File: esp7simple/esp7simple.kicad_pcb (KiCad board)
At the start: 2 copper layers, 13 parts, among them J1 Conn_01x02_Female, J2 , J3 , U1 ESP-07v2, U2 AMS1117-3.3

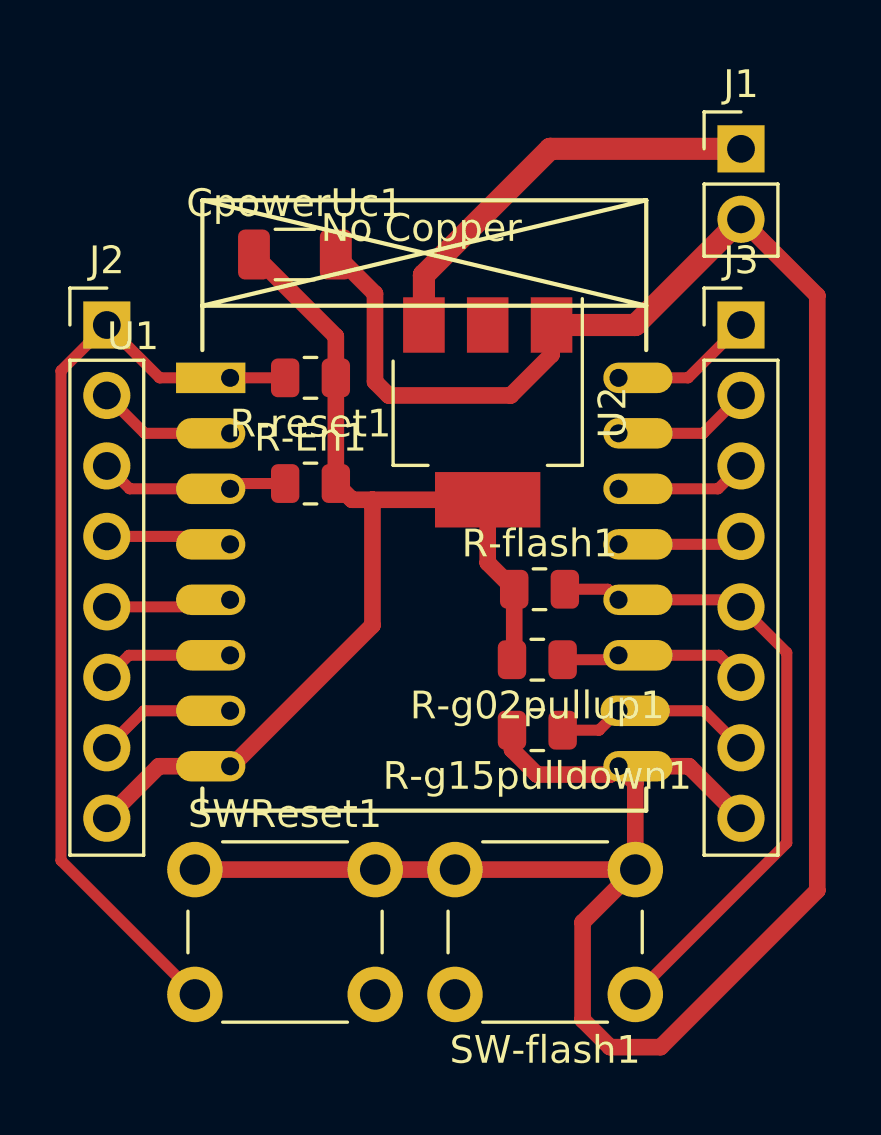
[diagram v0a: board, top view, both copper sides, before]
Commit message: add esp7 simple variant
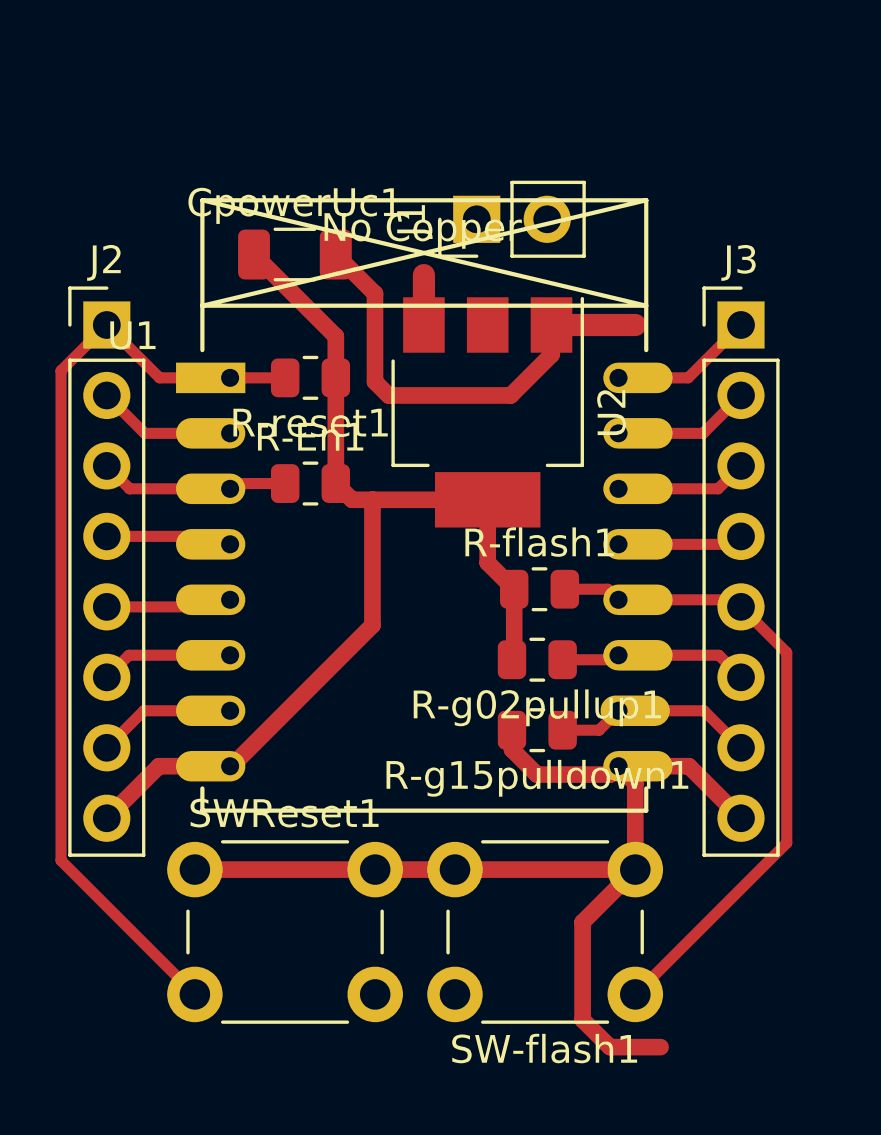
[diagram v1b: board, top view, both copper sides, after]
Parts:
- moved J1 9.86 mm to (154.9, 130.2), turned to 90 degrees
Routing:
- net GND: track 94.6 -> 55.9 mm
- net Net-(J1-Pad1): track 15.1 -> 1.80 mm
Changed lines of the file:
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@@
     (thickness 1.6)
     (drawings 0)
-    (tracks 86)
+    (tracks 80)
     (zones 0)
     (modules 13)
@@
   )
   (module Connector_PinHeader_2.54mm:PinHeader_1x02_P2.54mm_Vertical (layer F.Cu)
-    (at 164.465 127.635)
+    (at 154.94 130.175 90)
     (descr "Through hole straight pin header, 1x02, 2.54mm pitch, single row")
     (tags "Through hole pin header THT 1x02 2.54mm single row")
-    (fp_text reference J1 (at 0 -2.33) (layer F.SilkS)
-      (effects (font (size 1 1) (thickness 0.15)))
-    )
-    (fp_text value Conn_01x02_Female (at 2.54 6.35) (layer F.Fab) hide
+    (fp_text reference J1 (at 0 -2.33 90) (layer F.SilkS)
+      (effects (font (size 1 1) (thickness 0.15)))
+    )
+    (fp_text value Conn_01x02_Female (at 2.54 6.35 90) (layer F.Fab) hide
       (effects (font (size 1 1) (thickness 0.15)))
     )
@@
     (fp_line (start 1.27 -1.27) (end 1.27 3.81) (layer F.Fab) (width 0.1))
     (fp_line (start -0.635 -1.27) (end 1.27 -1.27) (layer F.Fab) (width 0.1))
-    (fp_text user %R (at 0 1.27 -270) (layer F.Fab)
-      (effects (font (size 1 1) (thickness 0.15)))
-    )
-    (pad 2 thru_hole oval (at 0 2.54) (size 1.7 1.7) (drill 1) (layers *.Cu *.Mask)
-      (net 1 GND))
-    (pad 1 thru_hole rect (at 0 0) (size 1.7 1.7) (drill 1) (layers *.Cu *.Mask)
+    (fp_text user %R (at 0 1.27) (layer F.Fab)
+      (effects (font (size 1 1) (thickness 0.15)))
+    )
+    (pad 2 thru_hole oval (at 0 2.54 90) (size 1.7 1.7) (drill 1) (layers *.Cu *.Mask)
+      (net 1 GND))
+    (pad 1 thru_hole rect (at 0 0 90) (size 1.7 1.7) (drill 1) (layers *.Cu *.Mask)
       (net 3 "Net-(J1-Pad1)"))
     (model ${KISYS3DMOD}/Connector_PinHeader_2.54mm.3dshapes/PinHeader_1x02_P2.54mm_Vertical.wrl
@@
       (effects (font (size 0.5 0.5) (thickness 0.08)))
     )
-    (pad 2 smd roundrect (at 0.9125 0 180) (size 1.025 1.4) (layers F.Cu F.Paste F.Mask) (roundrect_rratio 0.243902)
+    (pad 2 smd roundrect (at 0.9125 0 180) (size 1.025 1.4) (layers F.Cu F.Paste F.Mask) (roundrect_rratio 0.2439014634146341)
       (net 10 "Net-(J2-Pad1)"))
-    (pad 1 smd roundrect (at -0.9125 0 180) (size 1.025 1.4) (layers F.Cu F.Paste F.Mask) (roundrect_rratio 0.243902)
+    (pad 1 smd roundrect (at -0.9125 0 180) (size 1.025 1.4) (layers F.Cu F.Paste F.Mask) (roundrect_rratio 0.2439014634146341)
       (net 2 v3.3))
     (model ${KISYS3DMOD}/Resistor_SMD.3dshapes/R_0805_2012Metric.wrl
@@
       (effects (font (size 0.5 0.5) (thickness 0.08)))
     )
-    (pad 2 smd roundrect (at 0.9125 0 180) (size 1.025 1.4) (layers F.Cu F.Paste F.Mask) (roundrect_rratio 0.243902)
-      (net 1 GND))
-    (pad 1 smd roundrect (at -0.9125 0 180) (size 1.025 1.4) (layers F.Cu F.Paste F.Mask) (roundrect_rratio 0.243902)
+    (pad 2 smd roundrect (at 0.9125 0 180) (size 1.025 1.4) (layers F.Cu F.Paste F.Mask) (roundrect_rratio 0.2439014634146341)
+      (net 1 GND))
+    (pad 1 smd roundrect (at -0.9125 0 180) (size 1.025 1.4) (layers F.Cu F.Paste F.Mask) (roundrect_rratio 0.2439014634146341)
       (net 11 "Net-(J3-Pad7)"))
     (model ${KISYS3DMOD}/Resistor_SMD.3dshapes/R_0805_2012Metric.wrl
@@
       (effects (font (size 0.5 0.5) (thickness 0.08)))
     )
-    (pad 2 smd roundrect (at 0.9125 0 180) (size 1.025 1.4) (layers F.Cu F.Paste F.Mask) (roundrect_rratio 0.243902)
-      (net 2 v3.3))
-    (pad 1 smd roundrect (at -0.9125 0 180) (size 1.025 1.4) (layers F.Cu F.Paste F.Mask) (roundrect_rratio 0.243902)
+    (pad 2 smd roundrect (at 0.9125 0 180) (size 1.025 1.4) (layers F.Cu F.Paste F.Mask) (roundrect_rratio 0.2439014634146341)
+      (net 2 v3.3))
+    (pad 1 smd roundrect (at -0.9125 0 180) (size 1.025 1.4) (layers F.Cu F.Paste F.Mask) (roundrect_rratio 0.2439014634146341)
       (net 12 "Net-(J3-Pad6)"))
     (model ${KISYS3DMOD}/Resistor_SMD.3dshapes/R_0805_2012Metric.wrl
@@
       (effects (font (size 0.5 0.5) (thickness 0.08)))
     )
-    (pad 2 smd roundrect (at 0.9125 0) (size 1.025 1.4) (layers F.Cu F.Paste F.Mask) (roundrect_rratio 0.243902)
+    (pad 2 smd roundrect (at 0.9125 0) (size 1.025 1.4) (layers F.Cu F.Paste F.Mask) (roundrect_rratio 0.2439014634146341)
       (net 13 "Net-(J3-Pad5)"))
-    (pad 1 smd roundrect (at -0.9125 0) (size 1.025 1.4) (layers F.Cu F.Paste F.Mask) (roundrect_rratio 0.243902)
+    (pad 1 smd roundrect (at -0.9125 0) (size 1.025 1.4) (layers F.Cu F.Paste F.Mask) (roundrect_rratio 0.2439014634146341)
       (net 2 v3.3))
     (model ${KISYS3DMOD}/Resistor_SMD.3dshapes/R_0805_2012Metric.wrl
@@
       (effects (font (size 0.5 0.5) (thickness 0.08)))
     )
-    (pad 2 smd roundrect (at 0.9125 0) (size 1.025 1.4) (layers F.Cu F.Paste F.Mask) (roundrect_rratio 0.243902)
-      (net 2 v3.3))
-    (pad 1 smd roundrect (at -0.9125 0) (size 1.025 1.4) (layers F.Cu F.Paste F.Mask) (roundrect_rratio 0.243902)
+    (pad 2 smd roundrect (at 0.9125 0) (size 1.025 1.4) (layers F.Cu F.Paste F.Mask) (roundrect_rratio 0.2439014634146341)
+      (net 2 v3.3))
+    (pad 1 smd roundrect (at -0.9125 0) (size 1.025 1.4) (layers F.Cu F.Paste F.Mask) (roundrect_rratio 0.2439014634146341)
       (net 8 "Net-(J2-Pad3)"))
     (model ${KISYS3DMOD}/Resistor_SMD.3dshapes/R_0805_2012Metric.wrl
@@
       (effects (font (size 0.8 0.8) (thickness 0.12)))
     )
-    (pad 2 smd roundrect (at 1.475 0) (size 1.15 1.8) (layers F.Cu F.Paste F.Mask) (roundrect_rratio 0.217391)
-      (net 1 GND))
-    (pad 1 smd roundrect (at -1.475 0) (size 1.15 1.8) (layers F.Cu F.Paste F.Mask) (roundrect_rratio 0.217391)
+    (pad 2 smd roundrect (at 1.475 0) (size 1.15 1.8) (layers F.Cu F.Paste F.Mask) (roundrect_rratio 0.2173904347826087)
+      (net 1 GND))
+    (pad 1 smd roundrect (at -1.475 0) (size 1.15 1.8) (layers F.Cu F.Paste F.Mask) (roundrect_rratio 0.2173904347826087)
       (net 2 v3.3))
     (model ${KISYS3DMOD}/Capacitor_SMD.3dshapes/C_1206_3216Metric.wrl
@@
   (segment (start 162.59 149.89) (end 164.465 151.765) (width 0.6) (layer F.Cu) (net 1))
   (segment (start 160.05 149.89) (end 162.59 149.89) (width 0.6) (layer F.Cu) (net 1))
-  (segment (start 160.655 133.985) (end 164.465 130.175) (width 0.8) (layer F.Cu) (net 1))
   (segment (start 157.635 133.985) (end 160.655 133.985) (width 0.8) (layer F.Cu) (net 1))
   (segment (start 157.635 135.055002) (end 156.165002 136.525) (width 0.6) (layer F.Cu) (net 1))
@@
   (segment (start 156.21 149.29) (end 157.11001 150.19001) (width 0.6) (layer F.Cu) (net 1))
   (segment (start 156.21 148.59) (end 156.21 149.29) (width 0.6) (layer F.Cu) (net 1))
-  (segment (start 167.215011 132.925011) (end 164.465 130.175) (width 0.6) (layer F.Cu) (net 1))
-  (segment (start 167.215011 154.366991) (end 167.215011 132.925011) (width 0.6) (layer F.Cu) (net 1))
-  (segment (start 161.567001 160.015001) (end 167.215011 154.366991) (width 0.6) (layer F.Cu) (net 1))
   (segment (start 159.742999 160.015001) (end 161.567001 160.015001) (width 0.6) (layer F.Cu) (net 1))
   (segment (start 158.754999 159.027001) (end 159.742999 160.015001) (width 0.6) (layer F.Cu) (net 1))
@@
   (segment (start 151.18 140.285) (end 150.445 140.285) (width 0.6) (layer F.Cu) (net 2))
   (segment (start 155.335 140.285) (end 151.18 140.285) (width 0.6) (layer F.Cu) (net 2))
-  (segment (start 157.585 127.635) (end 164.465 127.635) (width 0.8) (layer F.Cu) (net 3))
-  (segment (start 153.035 132.185) (end 157.585 127.635) (width 0.8) (layer F.Cu) (net 3))
   (segment (start 153.035 133.985) (end 153.035 132.185) (width 0.8) (layer F.Cu) (net 3))
   (segment (start 144.21 147.89) (end 146.05 147.89) (width 0.25) (layer F.Cu) (net 4))
